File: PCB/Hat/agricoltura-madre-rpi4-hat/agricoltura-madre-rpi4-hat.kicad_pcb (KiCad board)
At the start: 4 copper layers, 106 x 85 mm, 78 parts, among them J1 Barrel_Jack, M1 MGM210P022JIA2R, M2 AG9900M, M3 25mm_FAN, M4 DummyPi, M5 LPA-C041301S-4, M6 SPSGRFC-915, SW1 TL3301NF260QG, SW2 EG1213, T1 0395121004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

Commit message: RPi version PSU
updated POE circuit with fixed footprint for rectifier diodes.
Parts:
- D2, D3: footprint growbox-KiCAD-Diodes:ABS210-13 -> AVR-KiCAD-Lib-Diodes:ABS210-13
- moved SW1 27.6 mm to (157.8, 107.0)
- moved R13 27.3 mm to (149.9, 69.0), turned to 90 degrees
- moved C16 24.1 mm to (147.3, 69.0), turned to 270 degrees
- moved T3 19.2 mm to (128.4, 53.0)
- moved T1 18.9 mm to (147.5, 53.0)
- moved R16 17.3 mm to (131.8, 69.0), turned to 90 degrees
- moved C19 16.4 mm to (148.6, 69.3), turned to 270 degrees
- moved R14 15.9 mm to (130.7, 69.0), turned to 90 degrees
- moved U2 14.7 mm to (148.6, 64.0), turned to 90 degrees
- moved U3 13.4 mm to (129.4, 64.0), turned to 90 degrees
- moved C17 13.2 mm to (128.1, 69.0), turned to 270 degrees
- moved R6 10.6 mm to (130.7, 59.0), turned to 90 degrees
- moved C18 9.25 mm to (129.4, 69.3), turned to 270 degrees
- moved R5 8.68 mm to (149.9, 59.0), turned to 90 degrees
- moved M6 7.71 mm to (132.3, 124.0), turned to 0 degrees
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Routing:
- net /Zigbee Radio /SWDIO_JTAG: track 26.6 -> 0.00 mm, vias 2 -> 0
- net /Zigbee Radio /SWCLK_JTAG: track 19.9 -> 0.00 mm, vias 2 -> 0
- net /Zigbee Radio /SWO_JTAG: track 19.7 -> 0.00 mm, vias 2 -> 0
- net /Zigbee Radio /RESETn: track 19.1 -> 0.00 mm
- net /Zigbee Radio /RF_RX: track 24.3 -> 7.78 mm
- net /Zigbee Radio /PTI_FRAME: track 12.5 -> 0.00 mm
- net /RPi 4 Main Schematic/RF_RX: track 21.8 -> 10.1 mm
- net /Zigbee Radio /PTI_DATA: track 7.08 -> 0.00 mm
- net /PoE and Power Supplies/POE_VB1: track 9.72 -> 12.4 mm
- net /PoE and Power Supplies/POE_VA1: track 10.1 -> 8.93 mm
- net +3V3: track 36.1 -> 35.2 mm, vias 20 -> 19
- net GND: vias 128 -> 120

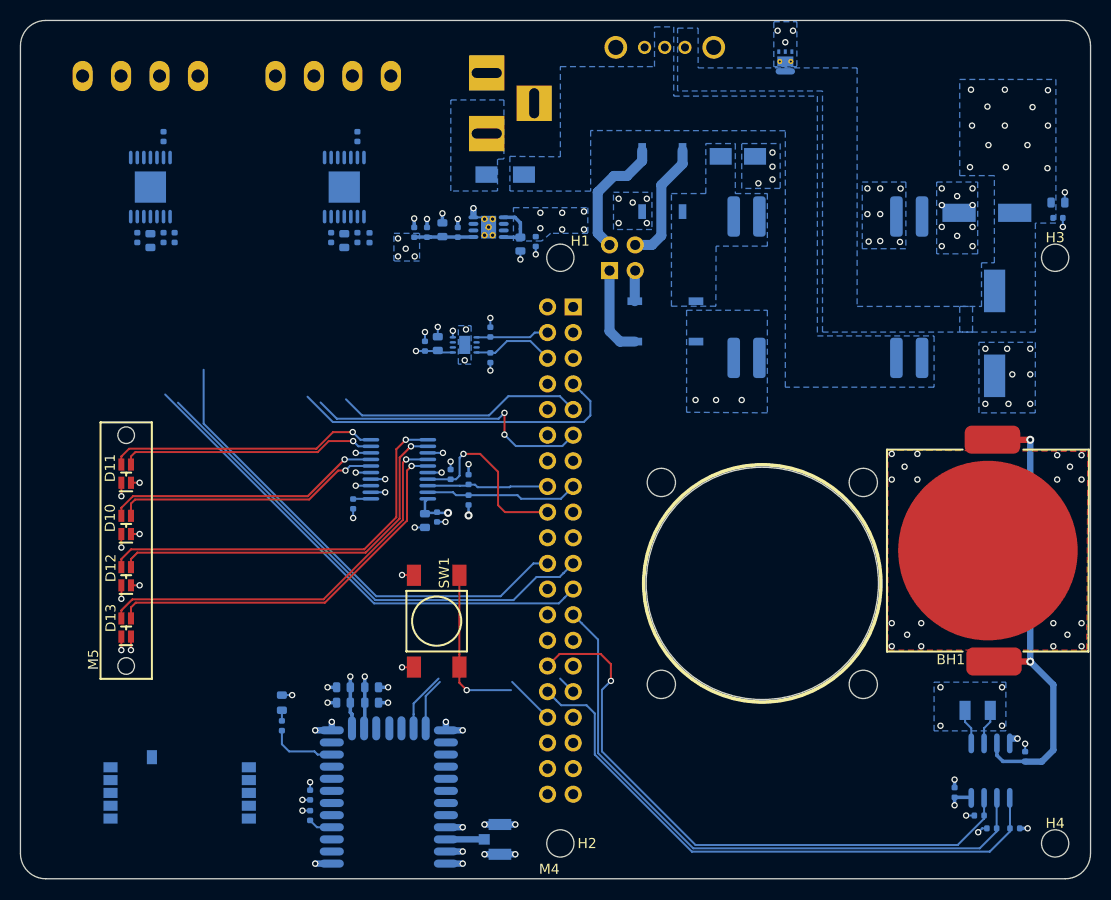
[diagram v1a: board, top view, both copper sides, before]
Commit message: KiCAD 8
Projected updated to KiCAD 8
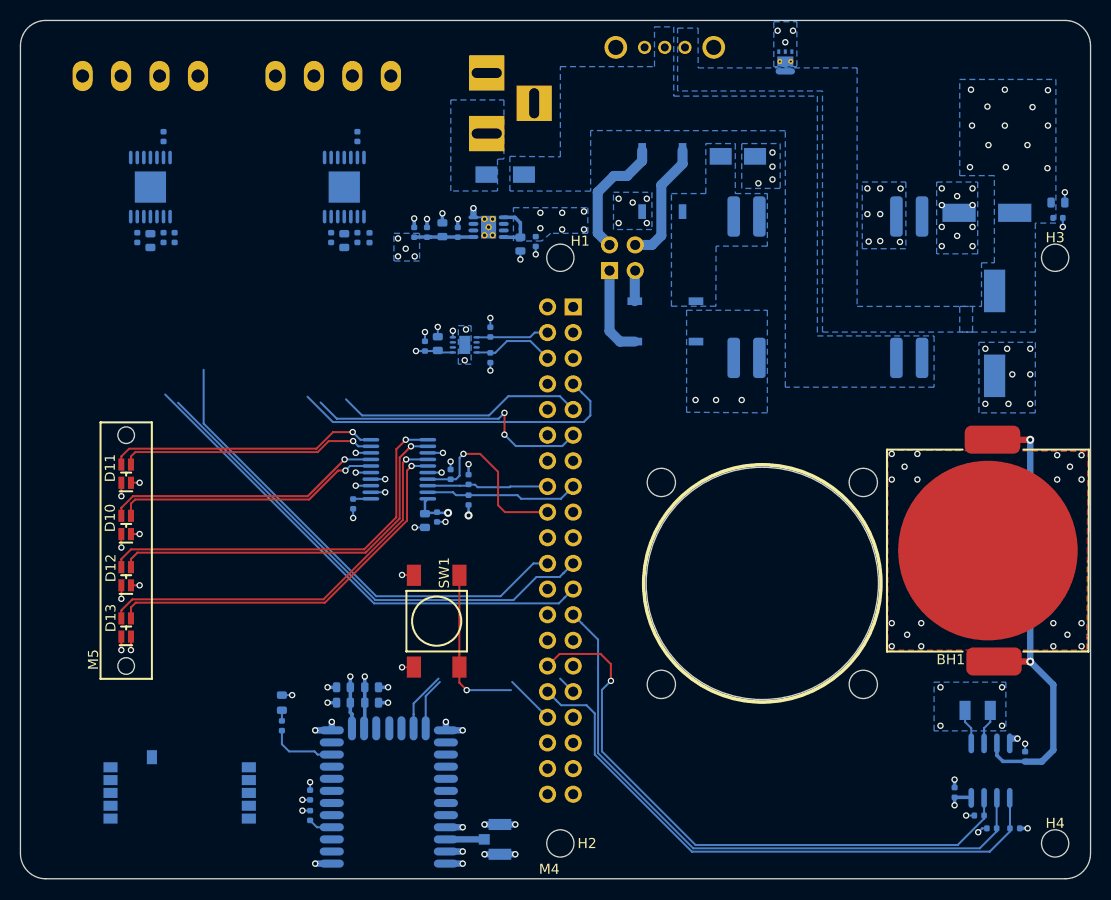
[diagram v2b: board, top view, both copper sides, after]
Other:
- net class Default removed
